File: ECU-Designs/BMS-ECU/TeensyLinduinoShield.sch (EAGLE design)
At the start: 9 parts, among them J1 ARDUINO_R3_SHIELD

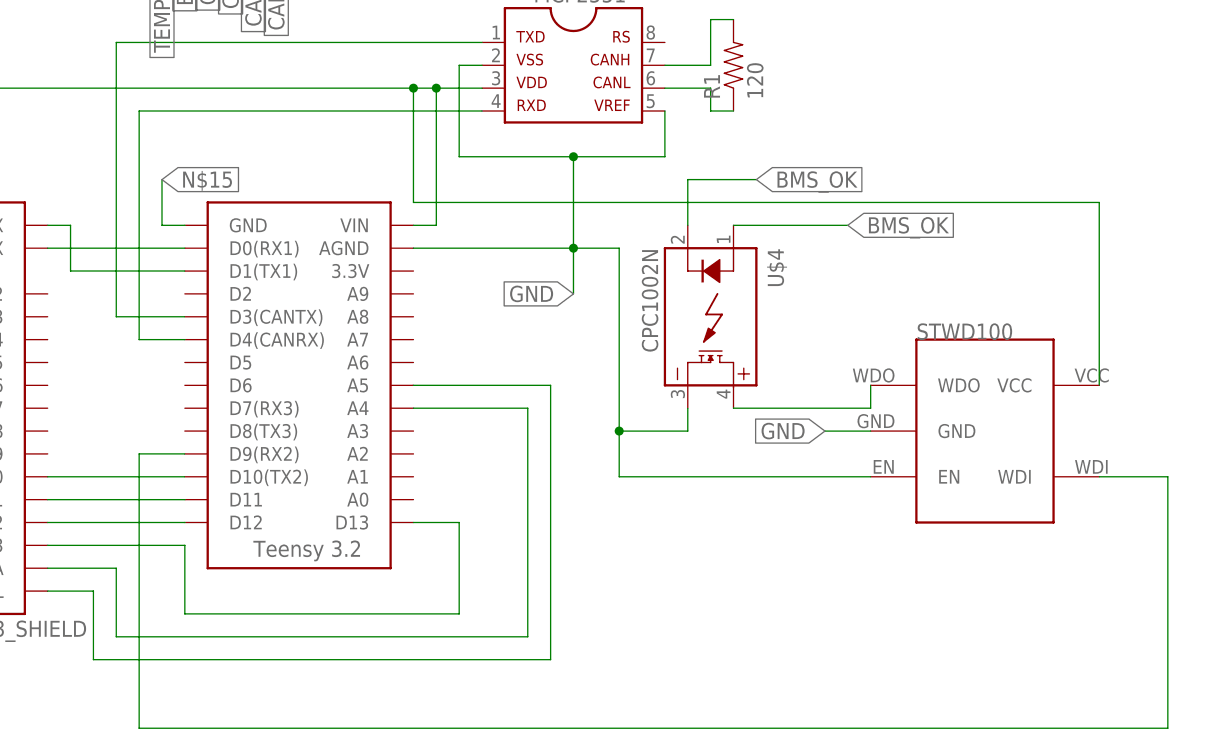
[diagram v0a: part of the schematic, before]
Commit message: BMS_OK signal connected so it can be driven by teensy
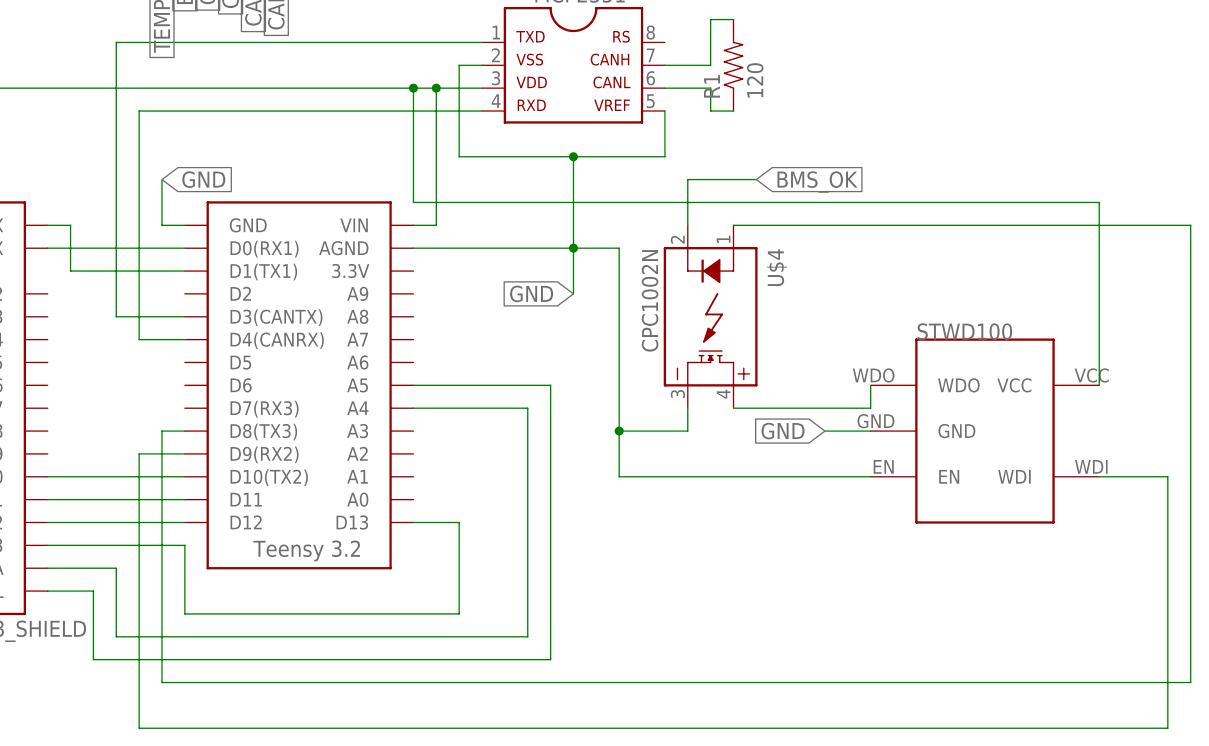
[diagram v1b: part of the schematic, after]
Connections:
- removed net N$15: U$1.GND
- new net N$16: U$1.D8(TX3), U$4.CONTROL+
- net BMS_OK: no longer U$4.CONTROL+
- net GND: now also U$1.GND
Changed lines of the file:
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@@
 <?xml version="1.0" encoding="utf-8"?>
 <!DOCTYPE eagle SYSTEM "eagle.dtd">
-<eagle version="8.1.0">
+<eagle version="7.7.0">
 <drawing>
 <settings>
@@
 <label x="139.7" y="55.88" size="1.778" layer="95" rot="R180" xref="yes"/>
 </segment>
+<segment>
+<pinref part="U$1" gate="G$1" pin="GND"/>
+<wire x1="96.52" y1="63.5" x2="93.98" y2="63.5" width="0.1524" layer="91"/>
+<wire x1="93.98" y1="63.5" x2="93.98" y2="68.58" width="0.1524" layer="91"/>
+<label x="93.98" y="68.58" size="1.778" layer="95" xref="yes"/>
+</segment>
 </net>
 <net name="CANH-OUT" class="0">
@@
 <wire x1="96.52" y1="104.14" x2="96.52" y2="99.06" width="0.1524" layer="91"/>
 <label x="96.52" y="99.06" size="1.778" layer="95" rot="R270" xref="yes"/>
-</segment>
-<segment>
-<pinref part="U$4" gate="G$1" pin="CONTROL+"/>
-<wire x1="157.48" y1="63.5" x2="170.18" y2="63.5" width="0.1524" layer="91"/>
-<label x="170.18" y="63.5" size="1.778" layer="95" xref="yes"/>
 </segment>
 <segment>
@@
 </segment>
 </net>
-<net name="N$15" class="0">
-<segment>
-<pinref part="U$1" gate="G$1" pin="GND"/>
-<wire x1="96.52" y1="63.5" x2="93.98" y2="63.5" width="0.1524" layer="91"/>
-<wire x1="93.98" y1="63.5" x2="93.98" y2="68.58" width="0.1524" layer="91"/>
-<label x="93.98" y="68.58" size="1.778" layer="95" xref="yes"/>
-</segment>
-</net>
+<net name="N$16" class="0">
+<segment>
+<pinref part="U$1" gate="G$1" pin="D8(TX3)"/>
+<wire x1="96.52" y1="40.64" x2="93.98" y2="40.64" width="0.1524" layer="91"/>
+<wire x1="93.98" y1="40.64" x2="93.98" y2="12.7" width="0.1524" layer="91"/>
+<wire x1="93.98" y1="12.7" x2="208.28" y2="12.7" width="0.1524" layer="91"/>
+<wire x1="208.28" y1="12.7" x2="208.28" y2="63.5" width="0.1524" layer="91"/>
+<pinref part="U$4" gate="G$1" pin="CONTROL+"/>
+<wire x1="208.28" y1="63.5" x2="157.48" y2="63.5" width="0.1524" layer="91"/>
+</segment>
+</net>

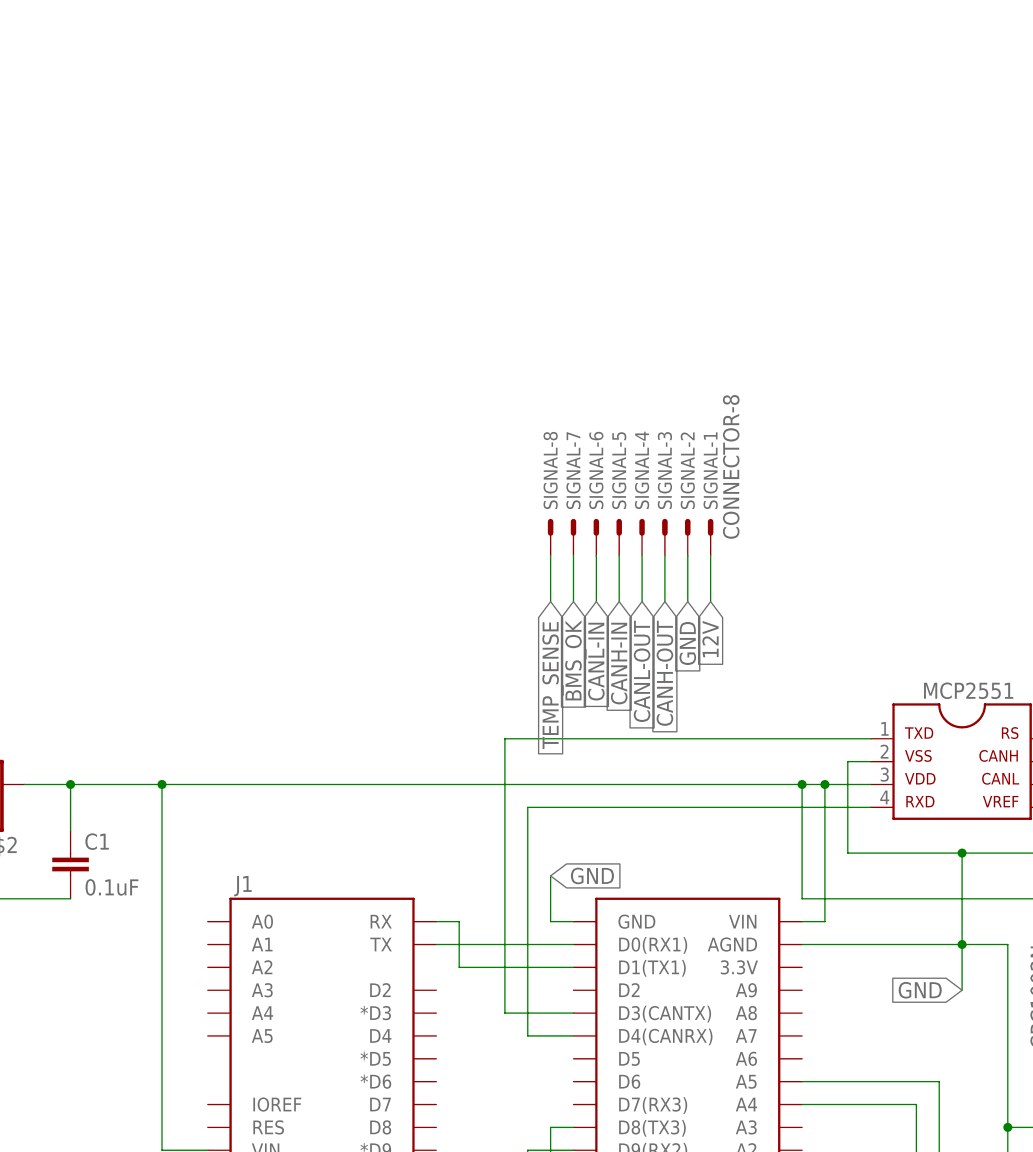
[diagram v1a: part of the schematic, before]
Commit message: Current sensor nanofit added. Connected to teensy and linduino
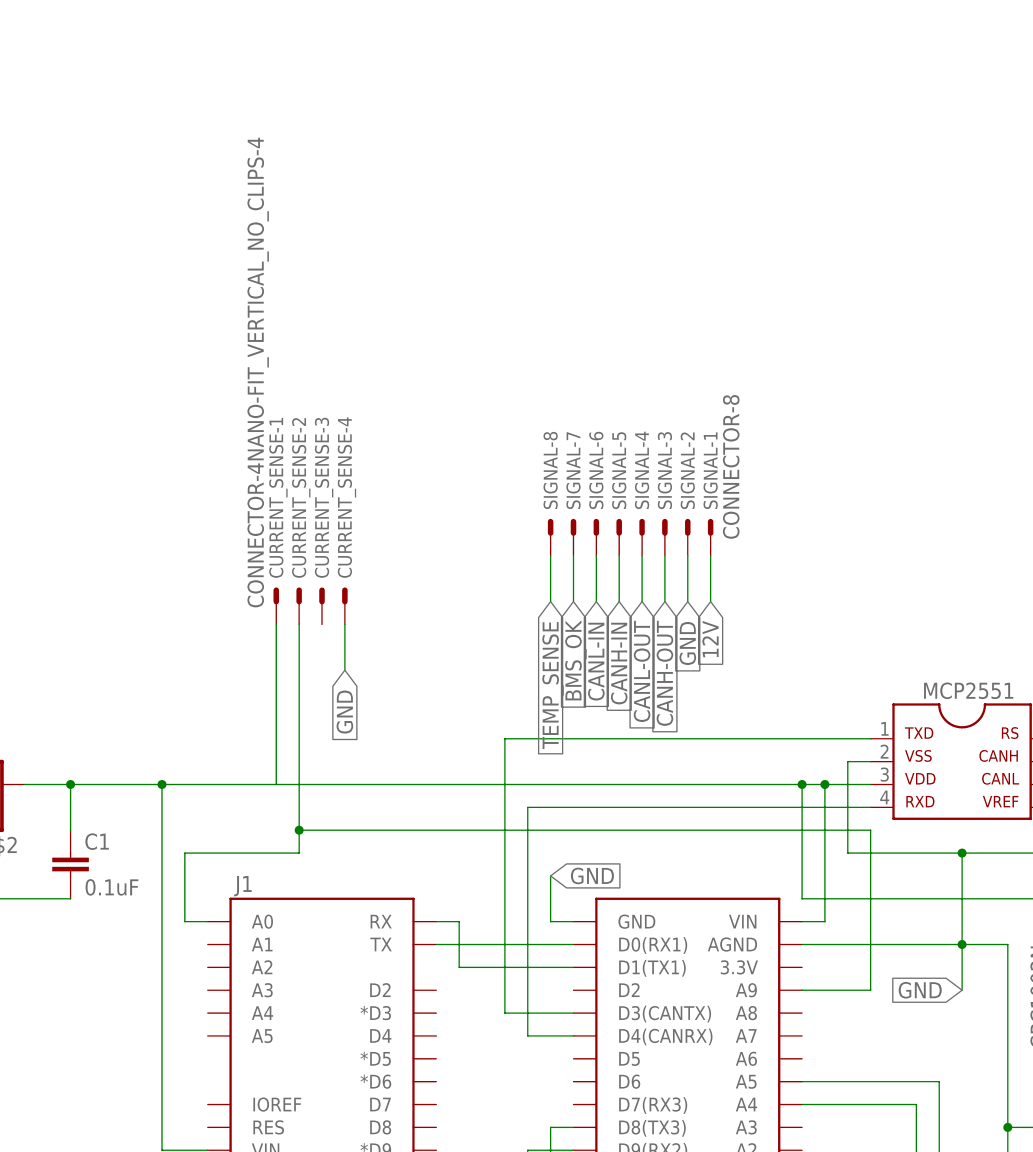
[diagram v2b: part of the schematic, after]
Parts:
- added CURRENT_SENSE: CONNECTOR-4NANO-FIT_VERTICAL_NO_CLIPS-4, HyTechDevices:CONNECTOR-4NANO-FIT_VERTICAL_NO_CLIPS-4
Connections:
- new net N$15: CURRENT_SENSE-2.S, J1.A0, U$1.A9
- net GND: now also CURRENT_SENSE-4.S
- net N$5: now also CURRENT_SENSE-1.S
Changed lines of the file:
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@@
 <grid distance="0.1" unitdist="inch" unit="inch" style="lines" multiple="1" display="no" altdistance="0.01" altunitdist="inch" altunit="inch"/>
 <layers>
-<layer number="1" name="Top" color="4" fill="1" visible="no" active="no"/>
-<layer number="2" name="Route2" color="1" fill="3" visible="no" active="no"/>
-<layer number="3" name="Route3" color="4" fill="3" visible="no" active="no"/>
-<layer number="14" name="Route14" color="1" fill="6" visible="no" active="no"/>
-<layer number="15" name="Route15" color="4" fill="6" visible="no" active="no"/>
-<layer number="16" name="Bottom" color="1" fill="1" visible="no" active="no"/>
-<layer number="17" name="Pads" color="2" fill="1" visible="no" active="no"/>
-<layer number="18" name="Vias" color="2" fill="1" visible="no" active="no"/>
-<layer number="19" name="Unrouted" color="6" fill="1" visible="no" active="no"/>
-<layer number="20" name="Dimension" color="15" fill="1" visible="no" active="no"/>
-<layer number="21" name="tPlace" color="7" fill="1" visible="no" active="no"/>
-<layer number="22" name="bPlace" color="7" fill="1" visible="no" active="no"/>
-<layer number="23" name="tOrigins" color="15" fill="1" visible="no" active="no"/>
-<layer number="24" name="bOrigins" color="15" fill="1" visible="no" active="no"/>
-<layer number="25" name="tNames" color="7" fill="1" visible="no" active="no"/>
-<layer number="26" name="bNames" color="7" fill="1" visible="no" active="no"/>
-<layer number="27" name="tValues" color="7" fill="1" visible="no" active="no"/>
-<layer number="28" name="bValues" color="7" fill="1" visible="no" active="no"/>
+<layer number="1" name="Top" color="4" fill="1" visible="yes" active="no"/>
+<layer number="2" name="Route2" color="1" fill="3" visible="yes" active="no"/>
+<layer number="3" name="Route3" color="4" fill="3" visible="yes" active="no"/>
+<layer number="14" name="Route14" color="1" fill="6" visible="yes" active="no"/>
+<layer number="15" name="Route15" color="4" fill="6" visible="yes" active="no"/>
+<layer number="16" name="Bottom" color="1" fill="1" visible="yes" active="no"/>
+<layer number="17" name="Pads" color="2" fill="1" visible="yes" active="no"/>
+<layer number="18" name="Vias" color="2" fill="1" visible="yes" active="no"/>
+<layer number="19" name="Unrouted" color="6" fill="1" visible="yes" active="no"/>
+<layer number="20" name="Dimension" color="15" fill="1" visible="yes" active="no"/>
+<layer number="21" name="tPlace" color="7" fill="1" visible="yes" active="no"/>
+<layer number="22" name="bPlace" color="7" fill="1" visible="yes" active="no"/>
+<layer number="23" name="tOrigins" color="15" fill="1" visible="yes" active="no"/>
+<layer number="24" name="bOrigins" color="15" fill="1" visible="yes" active="no"/>
+<layer number="25" name="tNames" color="7" fill="1" visible="yes" active="no"/>
+<layer number="26" name="bNames" color="7" fill="1" visible="yes" active="no"/>
+<layer number="27" name="tValues" color="7" fill="1" visible="yes" active="no"/>
+<layer number="28" name="bValues" color="7" fill="1" visible="yes" active="no"/>
 <layer number="29" name="tStop" color="7" fill="3" visible="no" active="no"/>
 <layer number="30" name="bStop" color="7" fill="6" visible="no" active="no"/>
@@
 <layer number="35" name="tGlue" color="7" fill="4" visible="no" active="no"/>
 <layer number="36" name="bGlue" color="7" fill="5" visible="no" active="no"/>
-<layer number="37" name="tTest" color="7" fill="1" visible="no" active="no"/>
-<layer number="38" name="bTest" color="7" fill="1" visible="no" active="no"/>
+<layer number="37" name="tTest" color="7" fill="1" visible="yes" active="no"/>
+<layer number="38" name="bTest" color="7" fill="1" visible="yes" active="no"/>
 <layer number="39" name="tKeepout" color="4" fill="11" visible="no" active="no"/>
 <layer number="40" name="bKeepout" color="1" fill="11" visible="no" active="no"/>
@@
 <layer number="44" name="Drills" color="7" fill="1" visible="no" active="no"/>
 <layer number="45" name="Holes" color="7" fill="1" visible="no" active="no"/>
-<layer number="46" name="Milling" color="3" fill="1" visible="no" active="no"/>
-<layer number="47" name="Measures" color="7" fill="1" visible="no" active="no"/>
-<layer number="48" name="Document" color="7" fill="1" visible="no" active="no"/>
-<layer number="49" name="Reference" color="7" fill="1" visible="no" active="no"/>
-<layer number="50" name="dxf" color="7" fill="1" visible="no" active="no"/>
-<layer number="51" name="tDocu" color="7" fill="1" visible="no" active="no"/>
-<layer number="52" name="bDocu" color="7" fill="1" visible="no" active="no"/>
-<layer number="53" name="tGND_GNDA" color="7" fill="9" visible="no" active="no"/>
-<layer number="54" name="bGND_GNDA" color="1" fill="9" visible="no" active="no"/>
-<layer number="56" name="wert" color="7" fill="1" visible="no" active="no"/>
-<layer number="57" name="tCAD" color="7" fill="1" visible="no" active="no"/>
-<layer number="59" name="tCarbon" color="7" fill="1" visible="no" active="no"/>
-<layer number="60" name="bCarbon" color="7" fill="1" visible="no" active="no"/>
+<layer number="46" name="Milling" color="3" fill="1" visible="yes" active="no"/>
+<layer number="47" name="Measures" color="7" fill="1" visible="yes" active="no"/>
+<layer number="48" name="Document" color="7" fill="1" visible="yes" active="no"/>
+<layer number="49" name="Reference" color="7" fill="1" visible="yes" active="no"/>
+<layer number="50" name="dxf" color="7" fill="1" visible="yes" active="no"/>
+<layer number="51" name="tDocu" color="7" fill="1" visible="yes" active="no"/>
+<layer number="52" name="bDocu" color="7" fill="1" visible="yes" active="no"/>
+<layer number="53" name="tGND_GNDA" color="7" fill="9" visible="yes" active="no"/>
+<layer number="54" name="bGND_GNDA" color="1" fill="9" visible="yes" active="no"/>
+<layer number="56" name="wert" color="7" fill="1" visible="yes" active="no"/>
+<layer number="57" name="tCAD" color="7" fill="1" visible="yes" active="no"/>
+<layer number="59" name="tCarbon" color="7" fill="1" visible="yes" active="no"/>
+<layer number="60" name="bCarbon" color="7" fill="1" visible="yes" active="no"/>
 <layer number="90" name="Modules" color="5" fill="1" visible="yes" active="yes"/>
 <layer number="91" name="Nets" color="2" fill="1" visible="yes" active="yes"/>
@@
 <part name="U$4" library="HyTechDevices" deviceset="CPC1002N" device=""/>
 <part name="SIGNAL" library="HyTechDevices" deviceset="CONNECTOR-8" device=""/>
+<part name="CURRENT_SENSE" library="HyTechDevices" deviceset="CONNECTOR-4" device="NANO-FIT_VERTICAL_NO_CLIPS-4"/>
 </parts>
 <sheets>
@@
 <instance part="SIGNAL" gate="-7" x="96.52" y="106.68" rot="MR90"/>
 <instance part="SIGNAL" gate="-8" x="93.98" y="106.68" rot="MR90"/>
+<instance part="CURRENT_SENSE" gate="-1" x="63.5" y="99.06" rot="R90"/>
+<instance part="CURRENT_SENSE" gate="-2" x="66.04" y="99.06" rot="R90"/>
+<instance part="CURRENT_SENSE" gate="-3" x="68.58" y="99.06" rot="R90"/>
+<instance part="CURRENT_SENSE" gate="-4" x="71.12" y="99.06" rot="R90"/>
 </instances>
 <busses>
@@
 <junction x="40.64" y="78.74"/>
 <pinref part="U$1" gate="G$1" pin="VIN"/>
-<wire x1="50.8" y1="78.74" x2="121.92" y2="78.74" width="0.1524" layer="91"/>
+<wire x1="50.8" y1="78.74" x2="60.96" y2="78.74" width="0.1524" layer="91"/>
+<wire x1="63.5" y1="78.74" x2="121.92" y2="78.74" width="0.1524" layer="91"/>
 <wire x1="121.92" y1="78.74" x2="124.46" y2="78.74" width="0.1524" layer="91"/>
 <wire x1="124.46" y1="78.74" x2="129.54" y2="78.74" width="0.1524" layer="91"/>
@@
 <wire x1="121.92" y1="66.04" x2="121.92" y2="78.74" width="0.1524" layer="91"/>
 <junction x="121.92" y="78.74"/>
+<pinref part="CURRENT_SENSE" gate="-1" pin="S"/>
+<wire x1="60.96" y1="78.74" x2="63.5" y2="78.74" width="0.1524" layer="91"/>
+<wire x1="63.5" y1="78.74" x2="63.5" y2="96.52" width="0.1524" layer="91"/>
 </segment>
 </net>
@@
 <label x="93.98" y="68.58" size="1.778" layer="95" xref="yes"/>
 </segment>
+<segment>
+<pinref part="CURRENT_SENSE" gate="-4" pin="S"/>
+<wire x1="71.12" y1="96.52" x2="71.12" y2="91.44" width="0.1524" layer="91"/>
+<label x="71.12" y="91.44" size="1.778" layer="95" rot="R270" xref="yes"/>
+</segment>
 </net>
 <net name="CANH-OUT" class="0">
@@
 </segment>
 </net>
+<net name="N$15" class="0">
+<segment>
+<pinref part="CURRENT_SENSE" gate="-2" pin="S"/>
+<wire x1="66.04" y1="96.52" x2="66.04" y2="73.66" width="0.1524" layer="91"/>
+<wire x1="66.04" y1="73.66" x2="66.04" y2="71.12" width="0.1524" layer="91"/>
+<wire x1="66.04" y1="71.12" x2="53.34" y2="71.12" width="0.1524" layer="91"/>
+<wire x1="53.34" y1="71.12" x2="53.34" y2="63.5" width="0.1524" layer="91"/>
+<pinref part="J1" gate="G$1" pin="A0"/>
+<wire x1="53.34" y1="63.5" x2="55.88" y2="63.5" width="0.1524" layer="91"/>
+<wire x1="66.04" y1="73.66" x2="129.54" y2="73.66" width="0.1524" layer="91"/>
+<wire x1="129.54" y1="73.66" x2="129.54" y2="55.88" width="0.1524" layer="91"/>
+<junction x="66.04" y="73.66"/>
+<pinref part="U$1" gate="G$1" pin="A9"/>
+<wire x1="129.54" y1="55.88" x2="121.92" y2="55.88" width="0.1524" layer="91"/>
+</segment>
+</net>
